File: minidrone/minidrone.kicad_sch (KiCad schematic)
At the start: 53 parts, among them J1 GATE, J2 OUT, J3 Conn_01x10, Q6 BC377, Q7 BC377, Q8 BC377, Q9 BC377, SW6 GATE, U1 TL072, U2 TL072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

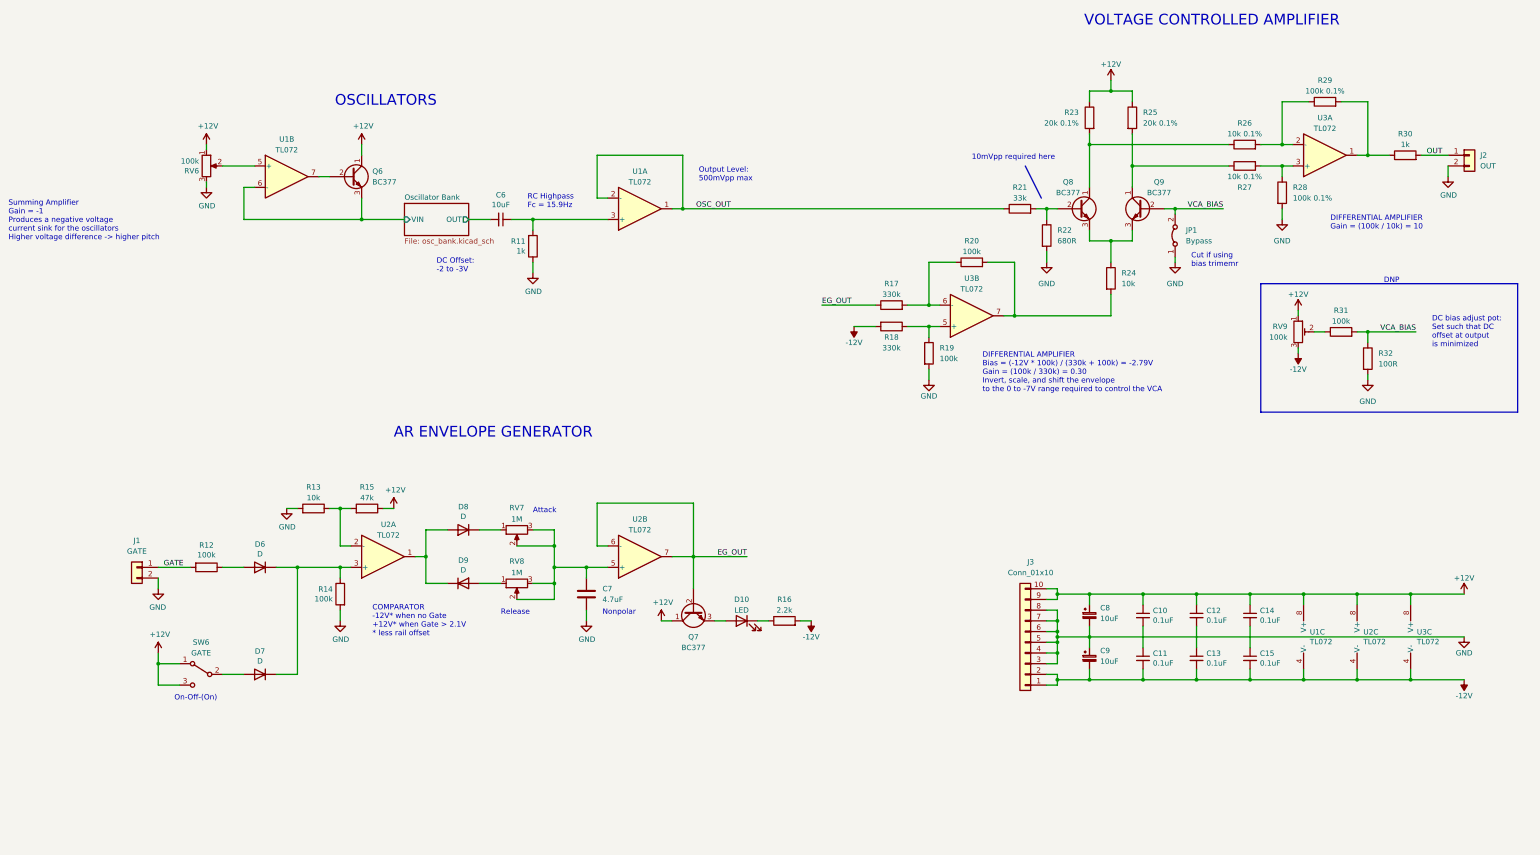
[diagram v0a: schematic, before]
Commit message: Correct pot footprints. continue layout
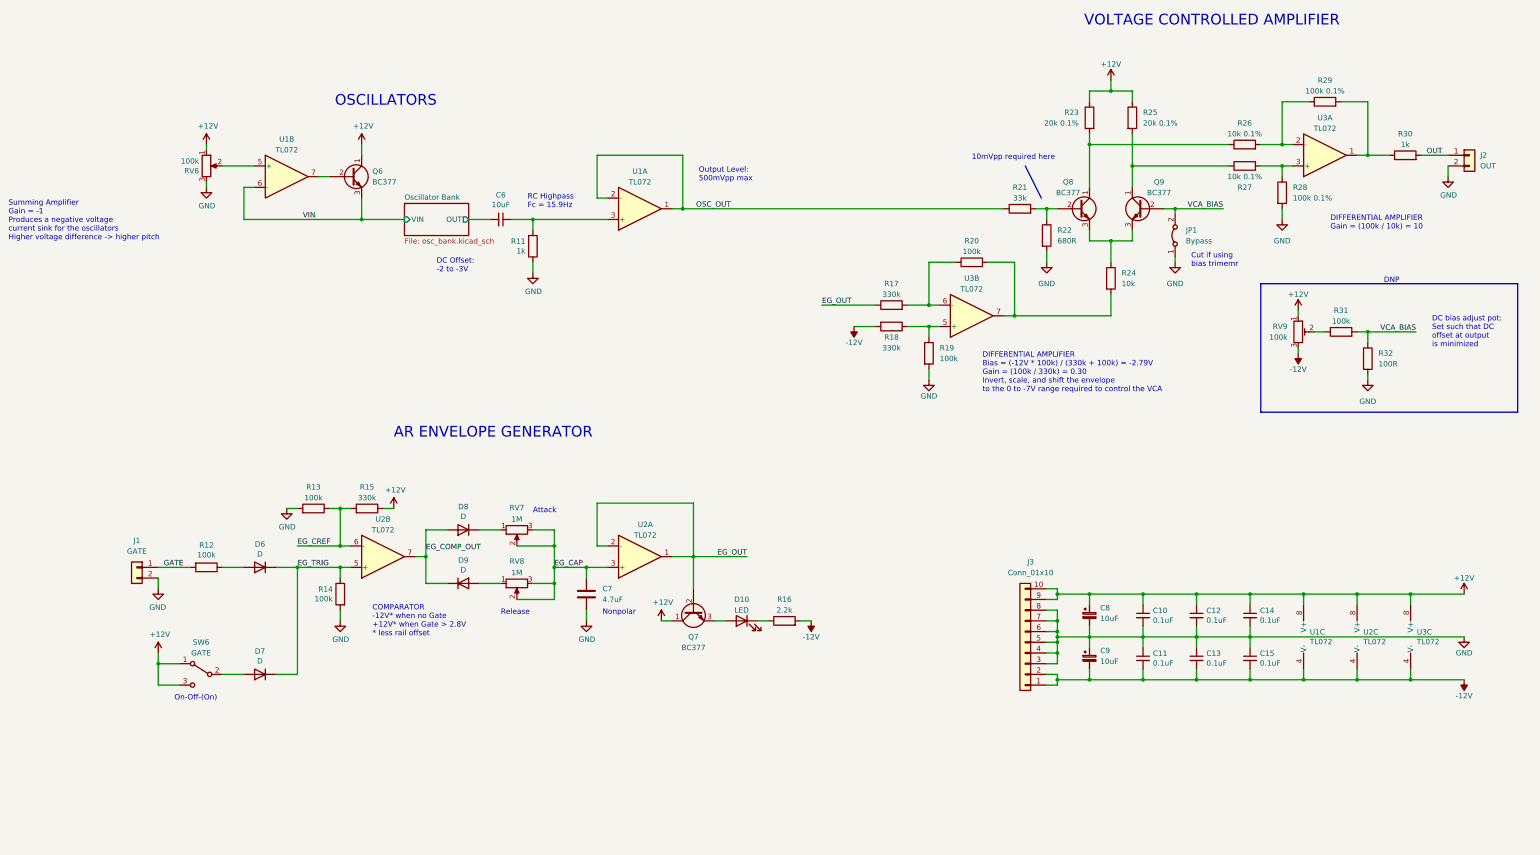
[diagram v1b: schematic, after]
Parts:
- R13: value 10k -> 100k
- R15: value 47k -> 330k
- R16: footprint Resistor_THT:R_Axial_DIN0207_L6.3mm_D2.5mm_P2.54mm_Vertical -> Resistor_THT:R_Axial_DIN0207_L6.3mm_D2.5mm_P10.16mm_Horizontal
- RV6: footprint Potentiometer_THT:Potentiometer_Bourns_PTV09A-1_Single_Vertical -> minidrone:Bourns_PVT09A
- RV7, RV8: footprint Potentiometer_THT:Potentiometer_Bourns_PTV09A-1_Single_Vertical -> minidrone:Bourns_PDB12-H
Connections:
- net EG_OUT: now also U2.1, U2.2 (-); no longer U2.6 (-), U2.7
- net GND: now also C10.2, C11.1, C12.2, C13.1, C14.2, C15.1
- net EG_COMP_OUT: now reaches D8.2 (A), D9.1 (K)
- net EG_COMP_OUT: now also U2.7; no longer U2.1
- net EG_CREF: now reaches R13.1, R15.2
- net EG_CREF: now also U2.6 (-); no longer U2.2 (-)
- net EG_TRIG: now reaches D6.1 (K), D7.1 (K), R14.1
- net EG_TRIG: now also U2.5 (+); no longer U2.3 (+)
- net EG_CAP: now reaches C7.1, RV7.2, RV7.3, RV8.2, RV8.3
- net EG_CAP: now also U2.3 (+); no longer U2.5 (+)
- net Oscillator Bank/VIN renamed VIN
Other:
- note added: "COMPARATOR -12V* when no Gate +12V* when Gate > 2.8V * less rail offset"
- note removed: "COMPARATOR -12V* when no Gate +12V* when Gate > 2.1V * less rail offset"
- moved on the sheet: U2A, U2B

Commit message: Continue layout
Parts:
- R11, R13, R17, R18, R19, R20, R24: footprint Resistor_THT:R_Axial_DIN0207_L6.3mm_D2.5mm_P2.54mm_Vertical -> Resistor_THT:R_Axial_DIN0207_L6.3mm_D2.5mm_P10.16mm_Horizontal
- R14: renamed from R15; footprint Resistor_THT:R_Axial_DIN0207_L6.3mm_D2.5mm_P2.54mm_Vertical -> Resistor_THT:R_Axial_DIN0207_L6.3mm_D2.5mm_P10.16mm_Horizontal
- renumbered R14 to R15
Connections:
- net at R18.1, R19.1: now also U3.3 (+); no longer U3.5 (+)
- net at R17.2, R20.1: now also U3.2 (-); no longer U3.6 (-)
- net at R20.2, R24.2: now also U3.1; no longer U3.7
- net at R26.2, R29.1: now also U3.6 (-); no longer U3.2 (-)
- net at R29.2, R30.1: now also U3.7; no longer U3.1
- net at R27.2, R28.1: now also U3.5 (+); no longer U3.3 (+)
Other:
- moved on the sheet: U3A, U3B

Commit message: Complete layout
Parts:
- R12, R15, R21, R22, R25, R26, R27, R28, R29, R30: footprint Resistor_THT:R_Axial_DIN0207_L6.3mm_D2.5mm_P2.54mm_Vertical -> Resistor_THT:R_Axial_DIN0207_L6.3mm_D2.5mm_P10.16mm_Horizontal
- R24: renamed from R23; footprint Resistor_THT:R_Axial_DIN0207_L6.3mm_D2.5mm_P2.54mm_Vertical -> Resistor_THT:R_Axial_DIN0207_L6.3mm_D2.5mm_P10.16mm_Horizontal
- renumbered R24 to R23
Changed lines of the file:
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@@
       (effects (font (size 1.27 1.27)) (justify left))
     )
-    (property "Footprint" "Resistor_THT:R_Axial_DIN0207_L6.3mm_D2.5mm_P2.54mm_Vertical" (id 2) (at 103.378 181.61 90)
+    (property "Footprint" "Resistor_THT:R_Axial_DIN0207_L6.3mm_D2.5mm_P10.16mm_Horizontal" (id 2) (at 103.378 181.61 90)
       (effects (font (size 1.27 1.27)) hide)
     )
@@
     (property "Reference" "R12" (id 0) (at 69.85 170.0022 90))
     (property "Value" "100k" (id 1) (at 69.85 172.3136 90))
-    (property "Footprint" "Resistor_THT:R_Axial_DIN0207_L6.3mm_D2.5mm_P2.54mm_Vertical" (id 2) (at 69.85 173.482 90)
+    (property "Footprint" "Resistor_THT:R_Axial_DIN0207_L6.3mm_D2.5mm_P10.16mm_Horizontal" (id 2) (at 69.85 173.482 90)
       (effects (font (size 1.27 1.27)) hide)
     )
@@
     (property "Reference" "R29" (id 0) (at 335.28 59.69 90))
     (property "Value" "100k 0.1%" (id 1) (at 335.28 62.23 90))
-    (property "Footprint" "Resistor_THT:R_Axial_DIN0207_L6.3mm_D2.5mm_P2.54mm_Vertical" (id 2) (at 335.28 66.548 90)
+    (property "Footprint" "Resistor_THT:R_Axial_DIN0207_L6.3mm_D2.5mm_P10.16mm_Horizontal" (id 2) (at 335.28 66.548 90)
       (effects (font (size 1.27 1.27)) hide)
     )
@@
     (property "Reference" "R26" (id 0) (at 316.23 69.85 90))
     (property "Value" "10k 0.1%" (id 1) (at 316.23 72.39 90))
-    (property "Footprint" "Resistor_THT:R_Axial_DIN0207_L6.3mm_D2.5mm_P2.54mm_Vertical" (id 2) (at 316.23 76.708 90)
+    (property "Footprint" "Resistor_THT:R_Axial_DIN0207_L6.3mm_D2.5mm_P10.16mm_Horizontal" (id 2) (at 316.23 76.708 90)
       (effects (font (size 1.27 1.27)) hide)
     )
@@
     (property "Reference" "R27" (id 0) (at 316.23 85.09 90))
     (property "Value" "10k 0.1%" (id 1) (at 316.23 82.55 90))
-    (property "Footprint" "Resistor_THT:R_Axial_DIN0207_L6.3mm_D2.5mm_P2.54mm_Vertical" (id 2) (at 316.23 78.232 90)
+    (property "Footprint" "Resistor_THT:R_Axial_DIN0207_L6.3mm_D2.5mm_P10.16mm_Horizontal" (id 2) (at 316.23 78.232 90)
       (effects (font (size 1.27 1.27)) hide)
     )
@@
       (effects (font (size 1.27 1.27)) (justify left))
     )
-    (property "Footprint" "Resistor_THT:R_Axial_DIN0207_L6.3mm_D2.5mm_P2.54mm_Vertical" (id 2) (at 287.782 68.58 90)
+    (property "Footprint" "Resistor_THT:R_Axial_DIN0207_L6.3mm_D2.5mm_P10.16mm_Horizontal" (id 2) (at 287.782 68.58 90)
       (effects (font (size 1.27 1.27)) hide)
     )
@@
   (symbol (lib_id "Device:R") (at 284.48 106.68 0) (unit 1)
     (in_bom yes) (on_board yes)
-    (property "Reference" "R24" (id 0) (at 287.02 105.41 0)
+    (property "Reference" "R23" (id 0) (at 287.02 105.41 0)
       (effects (font (size 1.27 1.27)) (justify left))
     )
@@
     (property "Reference" "R30" (id 0) (at 354.33 72.39 90))
     (property "Value" "1k" (id 1) (at 354.33 74.93 90))
-    (property "Footprint" "Resistor_THT:R_Axial_DIN0207_L6.3mm_D2.5mm_P2.54mm_Vertical" (id 2) (at 354.33 79.248 90)
+    (property "Footprint" "Resistor_THT:R_Axial_DIN0207_L6.3mm_D2.5mm_P10.16mm_Horizontal" (id 2) (at 354.33 79.248 90)
       (effects (font (size 1.27 1.27)) hide)
     )
@@
   (symbol (lib_id "Device:R") (at 279.4 68.58 0) (mirror y) (unit 1)
     (in_bom yes) (on_board yes)
-    (property "Reference" "R23" (id 0) (at 276.86 67.31 0)
+    (property "Reference" "R24" (id 0) (at 276.86 67.31 0)
       (effects (font (size 1.27 1.27)) (justify left))
     )
@@
       (effects (font (size 1.27 1.27)) (justify left))
     )
-    (property "Footprint" "Resistor_THT:R_Axial_DIN0207_L6.3mm_D2.5mm_P2.54mm_Vertical" (id 2) (at 281.178 68.58 90)
+    (property "Footprint" "Resistor_THT:R_Axial_DIN0207_L6.3mm_D2.5mm_P10.16mm_Horizontal" (id 2) (at 281.178 68.58 90)
       (effects (font (size 1.27 1.27)) hide)
     )
@@
       (effects (font (size 1.27 1.27)) (justify left))
     )
-    (property "Footprint" "Resistor_THT:R_Axial_DIN0207_L6.3mm_D2.5mm_P2.54mm_Vertical" (id 2) (at 323.342 86.36 90)
+    (property "Footprint" "Resistor_THT:R_Axial_DIN0207_L6.3mm_D2.5mm_P10.16mm_Horizontal" (id 2) (at 323.342 86.36 90)
       (effects (font (size 1.27 1.27)) hide)
     )
@@
     (property "Reference" "R21" (id 0) (at 262.89 85.09 90))
     (property "Value" "33k" (id 1) (at 262.89 87.63 90))
-    (property "Footprint" "Resistor_THT:R_Axial_DIN0207_L6.3mm_D2.5mm_P2.54mm_Vertical" (id 2) (at 262.89 91.948 90)
+    (property "Footprint" "Resistor_THT:R_Axial_DIN0207_L6.3mm_D2.5mm_P10.16mm_Horizontal" (id 2) (at 262.89 91.948 90)
       (effects (font (size 1.27 1.27)) hide)
     )
@@
       (effects (font (size 1.27 1.27)) (justify left))
     )
-    (property "Footprint" "Resistor_THT:R_Axial_DIN0207_L6.3mm_D2.5mm_P2.54mm_Vertical" (id 2) (at 267.462 96.52 90)
+    (property "Footprint" "Resistor_THT:R_Axial_DIN0207_L6.3mm_D2.5mm_P10.16mm_Horizontal" (id 2) (at 267.462 96.52 90)
       (effects (font (size 1.27 1.27)) hide)
     )
@@
     )
     (path "/00000000-0000-0000-0000-00006077f324"
-      (reference "R12") (unit 1) (value "100k") (footprint "Resistor_THT:R_Axial_DIN0207_L6.3mm_D2.5mm_P2.54mm_Vertical")
+      (reference "R12") (unit 1) (value "100k") (footprint "Resistor_THT:R_Axial_DIN0207_L6.3mm_D2.5mm_P10.16mm_Horizontal")
     )
     (path "/25b227de-5746-4ff3-95ea-9b35550438b3"
@@
     )
     (path "/00000000-0000-0000-0000-00006077f2f5"
-      (reference "R15") (unit 1) (value "100k") (footprint "Resistor_THT:R_Axial_DIN0207_L6.3mm_D2.5mm_P2.54mm_Vertical")
+      (reference "R15") (unit 1) (value "100k") (footprint "Resistor_THT:R_Axial_DIN0207_L6.3mm_D2.5mm_P10.16mm_Horizontal")
     )
     (path "/8505c997-d383-499d-a7b5-e8719aeb54f5"
@@
     )
     (path "/e1f16118-a2c4-4549-a045-798105ac5650"
-      (reference "R21") (unit 1) (value "33k") (footprint "Resistor_THT:R_Axial_DIN0207_L6.3mm_D2.5mm_P2.54mm_Vertical")
+      (reference "R21") (unit 1) (value "33k") (footprint "Resistor_THT:R_Axial_DIN0207_L6.3mm_D2.5mm_P10.16mm_Horizontal")
     )
     (path "/fb29bb2e-2194-4ad7-acf8-dc89f43e2bdb"
-      (reference "R22") (unit 1) (value "680R") (footprint "Resistor_THT:R_Axial_DIN0207_L6.3mm_D2.5mm_P2.54mm_Vertical")
+      (reference "R22") (unit 1) (value "680R") (footprint "Resistor_THT:R_Axial_DIN0207_L6.3mm_D2.5mm_P10.16mm_Horizontal")
+    )
+    (path "/a1e57bd1-ff8d-4f6f-b5bc-d8e21ebe9c29"
+      (reference "R23") (unit 1) (value "10k") (footprint "Resistor_THT:R_Axial_DIN0207_L6.3mm_D2.5mm_P10.16mm_Horizontal")
     )
     (path "/b6522ad3-0c36-4d24-b82c-94bc6005e0cc"
-      (reference "R23") (unit 1) (value "20k 0.1%") (footprint "Resistor_THT:R_Axial_DIN0207_L6.3mm_D2.5mm_P2.54mm_Vertical")
-    )
-    (path "/a1e57bd1-ff8d-4f6f-b5bc-d8e21ebe9c29"
-      (reference "R24") (unit 1) (value "10k") (footprint "Resistor_THT:R_Axial_DIN0207_L6.3mm_D2.5mm_P10.16mm_Horizontal")
+      (reference "R24") (unit 1) (value "20k 0.1%") (footprint "Resistor_THT:R_Axial_DIN0207_L6.3mm_D2.5mm_P10.16mm_Horizontal")
     )
     (path "/554be4dc-cf03-49f2-8514-7ec8175785dd"
-      (reference "R25") (unit 1) (value "20k 0.1%") (footprint "Resistor_THT:R_Axial_DIN0207_L6.3mm_D2.5mm_P2.54mm_Vertical")
+      (reference "R25") (unit 1) (value "20k 0.1%") (footprint "Resistor_THT:R_Axial_DIN0207_L6.3mm_D2.5mm_P10.16mm_Horizontal")
     )
     (path "/231f02c0-46ed-46b1-b35b-b4ad6db8e1b1"
-      (reference "R26") (unit 1) (value "10k 0.1%") (footprint "Resistor_THT:R_Axial_DIN0207_L6.3mm_D2.5mm_P2.54mm_Vertical")
+      (reference "R26") (unit 1) (value "10k 0.1%") (footprint "Resistor_THT:R_Axial_DIN0207_L6.3mm_D2.5mm_P10.16mm_Horizontal")
     )
     (path "/3ce7dd0a-8a45-41f8-b9a8-3cec3cff06e5"
-      (reference "R27") (unit 1) (value "10k 0.1%") (footprint "Resistor_THT:R_Axial_DIN0207_L6.3mm_D2.5mm_P2.54mm_Vertical")
+      (reference "R27") (unit 1) (value "10k 0.1%") (footprint "Resistor_THT:R_Axial_DIN0207_L6.3mm_D2.5mm_P10.16mm_Horizontal")
     )
     (path "/c05b4511-6709-4723-8923-3314049e94b1"
-      (reference "R28") (unit 1) (value "100k 0.1%") (footprint "Resistor_THT:R_Axial_DIN0207_L6.3mm_D2.5mm_P2.54mm_Vertical")
+      (reference "R28") (unit 1) (value "100k 0.1%") (footprint "Resistor_THT:R_Axial_DIN0207_L6.3mm_D2.5mm_P10.16mm_Horizontal")
     )
     (path "/1bd5140e-59da-4c1f-94a9-aba72cd350f1"
-      (reference "R29") (unit 1) (value "100k 0.1%") (footprint "Resistor_THT:R_Axial_DIN0207_L6.3mm_D2.5mm_P2.54mm_Vertical")
+      (reference "R29") (unit 1) (value "100k 0.1%") (footprint "Resistor_THT:R_Axial_DIN0207_L6.3mm_D2.5mm_P10.16mm_Horizontal")
     )
     (path "/a2bde4fa-8d26-4b7a-ab5a-f18f9b4248ee"
-      (reference "R30") (unit 1) (value "1k") (footprint "Resistor_THT:R_Axial_DIN0207_L6.3mm_D2.5mm_P2.54mm_Vertical")
+      (reference "R30") (unit 1) (value "1k") (footprint "Resistor_THT:R_Axial_DIN0207_L6.3mm_D2.5mm_P10.16mm_Horizontal")
     )
     (path "/09c347c6-94f0-48bb-849e-c3040533fdd3"

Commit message: Lay out front panel. WIP updating mainboard layout
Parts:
- removed D7: D, Diode_THT:D_DO-35_SOD27_P7.62mm_Horizontal, symbol Device:D
- removed R12: 100k, Resistor_THT:R_Axial_DIN0207_L6.3mm_D2.5mm_P10.16mm_Horizontal, symbol Device:R
- added J4: GATE, Connector_Molex:Molex_KK-254_AE-6410-02A_1x02_P2.54mm_Vertical, symbol Connector_Generic:Conn_01x02
- D6: value D -> 1N914
- D7: renamed from D8; value D -> 1N914
- D8: renamed from D9; value D -> 1N914
- J3: renamed from J1; value GATE -> EXT GATE
- SW6: value GATE -> GATE_LATCH; footprint modular:Switch_SPDT -> kosmo-lib:Switch_SPDT
- renumbered D10 to D9, J3 to J1
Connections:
- net GATE is gone; now on net EXT_GATE: J3.1 (Pin_1)
- net +12V: now also J4.1 (Pin_1); no longer SW6.1 (A)
- net EG_TRIG: now also SW6.2 (B), J4.2 (Pin_2)
- net CV: now reaches RV6.2, U1.5 (+)
- net EXT_GATE: now reaches D6.2 (A)
- net EG_CREF renamed EG_VTH
- no-connect marks 0 -> 1
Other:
- added sheet Front Panel (front_panel.kicad_sch)
- note added: "(On)-Off Keyswitch (Front Panel)"
- note added: "On-Off Toggle Switch"
- note removed: "On-Off-(On)"
- moved on the sheet: J3, R13, R14, SW6

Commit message: Complete initial layout
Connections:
- net EG_CAP: now also U2.5 (+); no longer U2.3 (+)
- net EG_COMP_OUT: now also U2.1; no longer U2.7
- net EG_OUT: now also U2.6 (-), U2.7; no longer U2.1, U2.2 (-)
- net EG_TRIG: now also U2.3 (+); no longer U2.5 (+)
- net EG_VTH: now also U2.2 (-); no longer U2.6 (-)
- net VCA_OUT: now reaches R29.2, R30.1, U3.7
- net VCA_DA_SIG: now reaches Q8.1 (C), R24.2, R26.1
- net VCA_IN: now reaches Q8.2 (B), R21.2, R22.1
- net VCA_CE: now reaches Q8.3 (E), Q9.3 (E), R23.1
- net VCA_DA_REF: now reaches Q9.1 (C), R25.2, R27.1
- net VCA_CV: now reaches R20.2, R23.2, U3.1
- net CV renamed PITCH
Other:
- moved on the sheet: J2, R21, R30, RV6, U2A, U2B
